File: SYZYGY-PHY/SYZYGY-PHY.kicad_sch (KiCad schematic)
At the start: 49 parts, among them J1 ARJM11C7-502-KB-EW2, J2 Conn_01x11, J3 Conn_01x02, J4 QTH-020-01-X-D-DP-A, U1 GPY111, U2 TXV0106BQBR, U3 TXV0106BQBR, Y1 Crystal_GND24

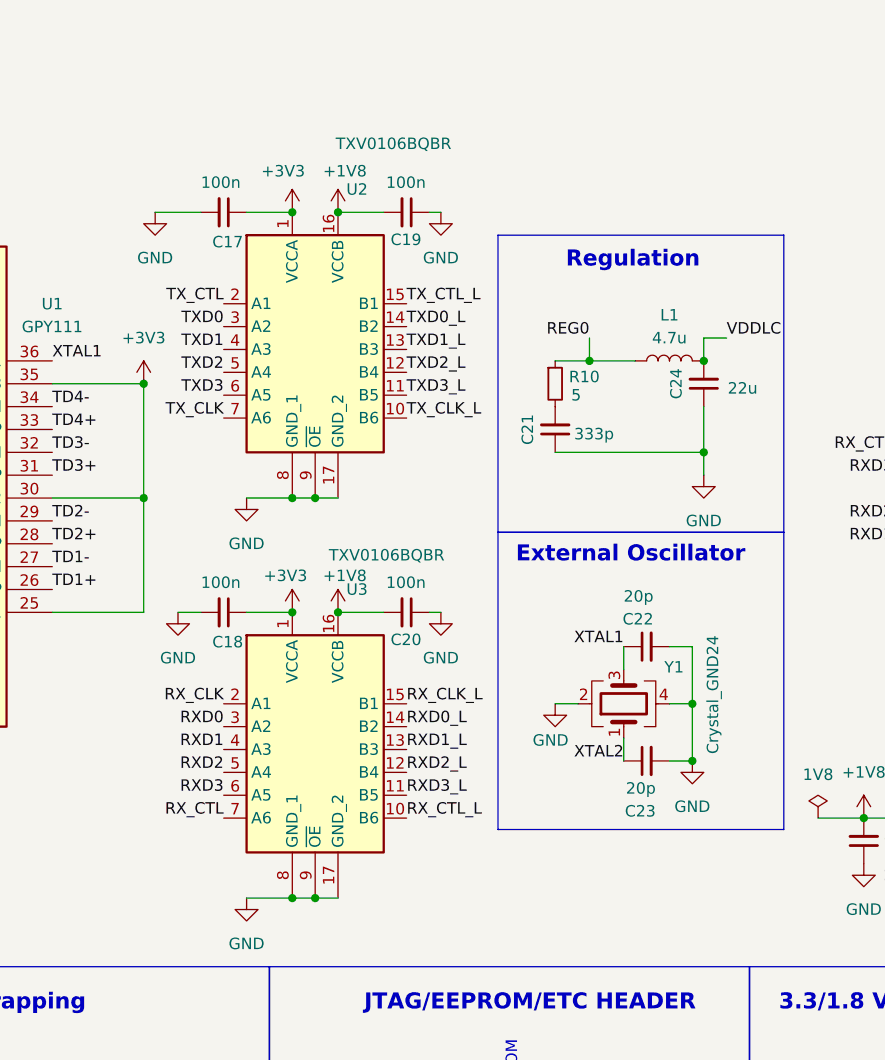
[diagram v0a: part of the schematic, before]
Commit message: busted: backwards level shifter
This snapshot updates the pin assignments such that our TX level shifter
fails the ERC, and then fixes that by flipping it in the schematic.

It also pulls all the updated details from the schematic into the
layout, which does not pass the DRC.
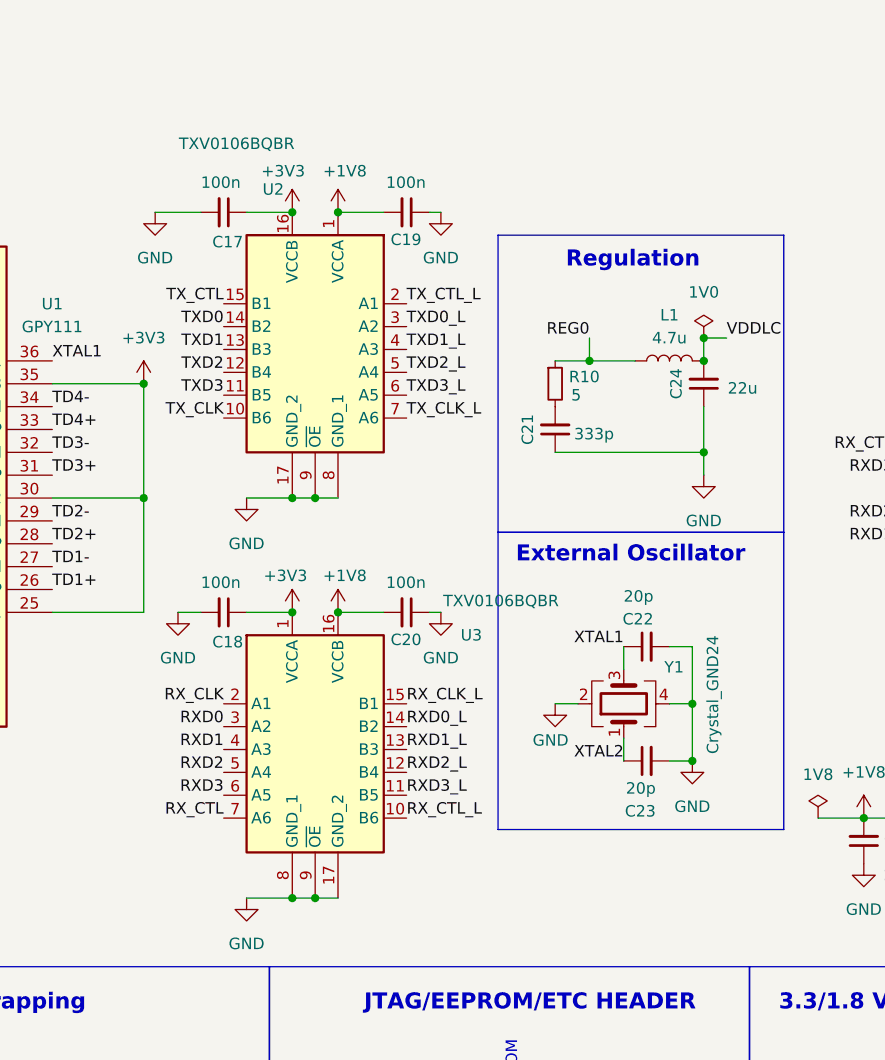
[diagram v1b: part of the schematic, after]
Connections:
- net +1V8: now also U2.1 (VCCA); no longer U2.16 (VCCB)
- net +3V3: now also U2.16 (VCCB); no longer U2.1 (VCCA)
- net TXD0: now also U2.14 (B2); no longer U2.3 (A2)
- net TXD0_L: now also U2.3 (A2); no longer U2.14 (B2)
- net TXD1: now also U2.13 (B3); no longer U2.4 (A3)
- net TXD1_L: now also U2.4 (A3); no longer U2.13 (B3)
- net TXD2: now also U2.12 (B4); no longer U2.5 (A4)
- net TXD2_L: now also U2.5 (A4); no longer U2.12 (B4)
- net TXD3: now also U2.11 (B5); no longer U2.6 (A5)
- net TXD3_L: now also U2.6 (A5); no longer U2.11 (B5)
- net TX_CLK: now also U2.10 (B6); no longer U2.7 (A6)
- net TX_CLK_L: now also U2.7 (A6); no longer U2.10 (B6)
- net TX_CTL: now also U2.15 (B1); no longer U2.2 (A1)
- net TX_CTL_L: now also U2.2 (A1); no longer U2.15 (B1)
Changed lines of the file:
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@@
 	)
 	(junction
-		(at 173.99 111.76)
+		(at 171.45 67.31)
 		(diameter 0)
 		(color 0 0 0 0)
@@
 	)
 	(junction
-		(at 171.45 67.31)
-		(diameter 0)
-		(color 0 0 0 0)
-	)
-	(junction
-		(at 176.53 80.01)
+		(at 140.97 137.16)
 		(diameter 0)
 		(color 0 0 0 0)
 	)
 	(junction
-		(at 140.97 137.16)
+		(at 80.01 31.75)
 		(diameter 0)
 		(color 0 0 0 0)
 	)
 	(junction
-		(at 80.01 31.75)
+		(at 73.66 31.75)
 		(diameter 0)
 		(color 0 0 0 0)
 	)
 	(junction
-		(at 73.66 31.75)
+		(at 173.99 111.76)
 		(diameter 0)
 		(color 0 0 0 0)
@@
 	)
 	(junction
-		(at 173.99 67.31)
+		(at 62.23 87.63)
 		(diameter 0)
 		(color 0 0 0 0)
 	)
 	(junction
-		(at 62.23 87.63)
+		(at 217.17 52.07)
 		(diameter 0)
 		(color 0 0 0 0)
 	)
 	(junction
-		(at 217.17 52.07)
+		(at 176.53 80.01)
 		(diameter 0)
 		(color 0 0 0 0)
@@
 	)
 	(junction
+		(at 171.45 35.56)
+		(diameter 0)
+		(color 0 0 0 0)
+	)
+	(junction
 		(at 60.96 26.67)
 		(diameter 0)
@@
 	)
 	(junction
-		(at 171.45 35.56)
-		(diameter 0)
-		(color 0 0 0 0)
-	)
-	(junction
 		(at 41.91 26.67)
 		(diameter 0)
@@
 	)
 	(junction
-		(at 176.53 35.56)
+		(at 217.17 49.53)
 		(diameter 0)
 		(color 0 0 0 0)
@@
 	)
 	(junction
+		(at 173.99 67.31)
+		(diameter 0)
+		(color 0 0 0 0)
+	)
+	(junction
 		(at 171.45 80.01)
 		(diameter 0)
@@
 	)
 	(junction
+		(at 176.53 35.56)
+		(diameter 0)
+		(color 0 0 0 0)
+	)
+	(junction
 		(at 118.11 154.94)
 		(diameter 0)
@@
 	(wire
 		(pts
-			(xy 171.45 111.76) (xy 173.99 111.76)
-		)
-		(stroke
-			(width 0)
-			(type default)
-		)
-	)
-	(wire
-		(pts
 			(xy 274.32 97.79) (xy 274.32 102.87)
 		)
@@
 	(wire
 		(pts
-			(xy 173.99 111.76) (xy 176.53 111.76)
-		)
-		(stroke
-			(width 0)
-			(type default)
-		)
-	)
-	(wire
-		(pts
 			(xy 156.21 35.56) (xy 161.29 35.56)
 		)
@@
 	(wire
 		(pts
+			(xy 173.99 111.76) (xy 176.53 111.76)
+		)
+		(stroke
+			(width 0)
+			(type default)
+		)
+	)
+	(wire
+		(pts
 			(xy 166.37 80.01) (xy 171.45 80.01)
 		)
@@
 	(wire
 		(pts
-			(xy 171.45 67.31) (xy 173.99 67.31)
+			(xy 173.99 67.31) (xy 176.53 67.31)
 		)
 		(stroke
@@
 	(wire
 		(pts
+			(xy 171.45 67.31) (xy 173.99 67.31)
+		)
+		(stroke
+			(width 0)
+			(type default)
+		)
+	)
+	(wire
+		(pts
 			(xy 114.3 97.79) (xy 114.3 113.03)
 		)
@@
 	(wire
 		(pts
-			(xy 173.99 67.31) (xy 176.53 67.31)
+			(xy 71.12 120.65) (xy 71.12 123.19)
 		)
 		(stroke
@@
 	(wire
 		(pts
-			(xy 71.12 120.65) (xy 71.12 123.19)
+			(xy 116.84 34.29) (xy 116.84 26.67)
 		)
 		(stroke
@@
 	(wire
 		(pts
-			(xy 116.84 34.29) (xy 116.84 26.67)
+			(xy 118.11 154.94) (xy 118.11 158.75)
 		)
 		(stroke
@@
 	(wire
 		(pts
-			(xy 118.11 154.94) (xy 118.11 158.75)
+			(xy 171.45 111.76) (xy 173.99 111.76)
 		)
 		(stroke
@@
 	(symbol
 		(lib_id "TXV0106BQBR:TXV0106BQBR")
-		(at 161.29 90.17 0)
+		(at 173.99 95.25 0)
 		(unit 1)
 		(exclude_from_sim no)
@@
 		(dnp no)
 		(property "Reference" "U3"
-			(at 177.4541 77.47 0)
+			(at 190.1541 82.55 0)
 			(effects
 				(font
@@
 		)
 		(property "Value" "TXV0106BQBR"
-			(at 175.514 73.66 0)
+			(at 188.214 78.74 0)
 			(effects
 				(font
@@
 		)
 		(property "Footprint" "local:TXV0106BQBR"
-			(at 182.88 174.93 0)
+			(at 195.58 180.01 0)
 			(effects
 				(font
@@
 		)
 		(property "Datasheet" "https://www.ti.com/lit/ds/symlink/txv0106.pdf?ts=1710334541958&ref_url=https%253A%252F%252Fwww.ti.com%252Fproduct%252FTXV0106%253FkeyMatch%253DTXV"
-			(at 182.88 274.93 0)
+			(at 195.58 280.01 0)
 			(effects
 				(font
@@
 		)
 		(property "Description" "Voltage Level Translator Unidirectional 1 Circuit 6 Channel 500Mbps 16-WQFN (2.5x3.5)"
-			(at 161.29 90.17 0)
+			(at 173.99 95.25 0)
 			(effects
 				(font
@@
 		)
 		(property "Height" "0.8"
-			(at 182.88 474.93 0)
+			(at 195.58 480.01 0)
 			(effects
 				(font
@@
 		)
 		(property "Mouser Part Number" "595-TXV0106BQBR"
-			(at 182.88 574.93 0)
+			(at 195.58 580.01 0)
 			(effects
 				(font
@@
 		)
 		(property "Mouser Price/Stock" "https://www.mouser.co.uk/ProductDetail/Texas-Instruments/TXV0106BQBR?qs=mELouGlnn3c1YOKCKwursg%3D%3D"
-			(at 182.88 674.93 0)
+			(at 195.58 680.01 0)
 			(effects
 				(font
@@
 		)
 		(property "Manufacturer_Name" "Texas Instruments"
-			(at 182.88 774.93 0)
+			(at 195.58 780.01 0)
 			(effects
 				(font
@@
 		)
 		(property "Manufacturer_Part_Number" "TXV0106BQBR"
-			(at 182.88 874.93 0)
+			(at 195.58 880.01 0)
 			(effects
 				(font
@@
 	(symbol
 		(lib_id "TXV0106BQBR:TXV0106BQBR")
-		(at 161.29 45.72 0)
+		(at 173.99 50.8 0)
+		(mirror y)
 		(unit 1)
 		(exclude_from_sim no)
@@
 		(dnp no)
 		(property "Reference" "U2"
-			(at 177.4541 33.02 0)
+			(at 170.5259 33.02 0)
 			(effects
 				(font
@@
 		)
 		(property "Value" "TXV0106BQBR"
-			(at 176.276 27.94 0)
+			(at 171.704 27.94 0)
 			(effects
 				(font
@@
 		)
 		(property "Footprint" "local:TXV0106BQBR"
-			(at 182.88 130.48 0)
+			(at 152.4 135.56 0)
 			(effects
 				(font
@@
 		)
 		(property "Datasheet" "https://www.ti.com/lit/ds/symlink/txv0106.pdf?ts=1710334541958&ref_url=https%253A%252F%252Fwww.ti.com%252Fproduct%252FTXV0106%253FkeyMatch%253DTXV"
-			(at 182.88 230.48 0)
+			(at 152.4 235.56 0)
 			(effects
 				(font
@@
 		)
 		(property "Description" "Voltage Level Translator Unidirectional 1 Circuit 6 Channel 500Mbps 16-WQFN (2.5x3.5)"
-			(at 161.29 45.72 0)
+			(at 174.244 49.53 0)
 			(effects
 				(font
@@
 		)
 		(property "Height" "0.8"
-			(at 182.88 430.48 0)
+			(at 152.4 435.56 0)
 			(effects
 				(font
@@
 		)
 		(property "Mouser Part Number" "595-TXV0106BQBR"
-			(at 182.88 530.48 0)
+			(at 152.4 535.56 0)
 			(effects
 				(font
@@
 		)
 		(property "Mouser Price/Stock" "https://www.mouser.co.uk/ProductDetail/Texas-Instruments/TXV0106BQBR?qs=mELouGlnn3c1YOKCKwursg%3D%3D"
-			(at 182.88 630.48 0)
+			(at 152.4 635.56 0)
 			(effects
 				(font
@@
 		)
 		(property "Manufacturer_Name" "Texas Instruments"
-			(at 182.88 730.48 0)
+			(at 152.4 735.56 0)
 			(effects
 				(font
@@
 		)
 		(property "Manufacturer_Part_Number" "TXV0106BQBR"
-			(at 182.88 830.48 0)
+			(at 152.4 835.56 0)
 			(effects
 				(font
@@
 					(unit 1)
 				)
+			)
+		)
+	)
+	(symbol
+		(lib_id "power:PWR_FLAG")
+		(at 217.17 49.53 0)
+		(unit 1)
+		(exclude_from_sim no)
+		(in_bom yes)
+		(on_board yes)
+		(dnp no)
+		(fields_autoplaced yes)
+		(property "Reference" "#FLG06"
+			(at 217.17 47.625 0)
+			(effects
+				(font
+					(size 1.27 1.27)
+				)
+				(hide yes)
+			)
+		)
+		(property "Value" "1V0"
+			(at 217.17 44.45 0)
+			(effects
+				(font
+					(size 1.27 1.27)
+				)
+			)
+		)
+		(property "Footprint" ""
+			(at 217.17 49.53 0)
+			(effects
+				(font
+					(size 1.27 1.27)
+				)
+				(hide yes)
+			)
+		)
+		(property "Datasheet" "~"
+			(at 217.17 49.53 0)
+			(effects
+				(font
+					(size 1.27 1.27)
+				)
+				(hide yes)
+			)
+		)
+		(property "Description" "Special symbol for telling ERC where power comes from"
+			(at 217.17 49.53 0)
+			(effects
+				(font
+					(size 1.27 1.27)
+				)
+				(hide yes)
+			)
+		)
+		(pin "1"
+		)
+		(instances
+			(project ""
+				(path "/cd7d6255-0cd2-43fc-ba6e-5ac7b6205d5d"
+					(reference "#FLG06")
+					(unit 1)
+				)

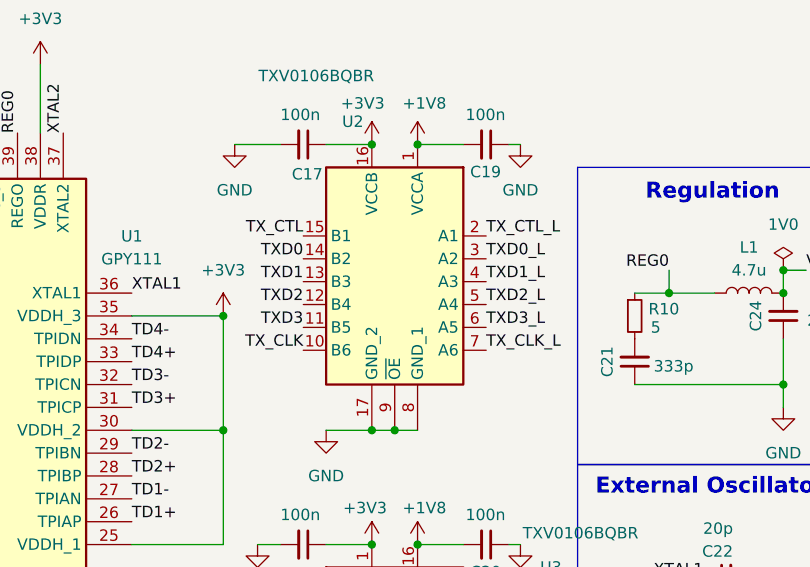
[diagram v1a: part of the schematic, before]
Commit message: flipping the level shifter adding some labels
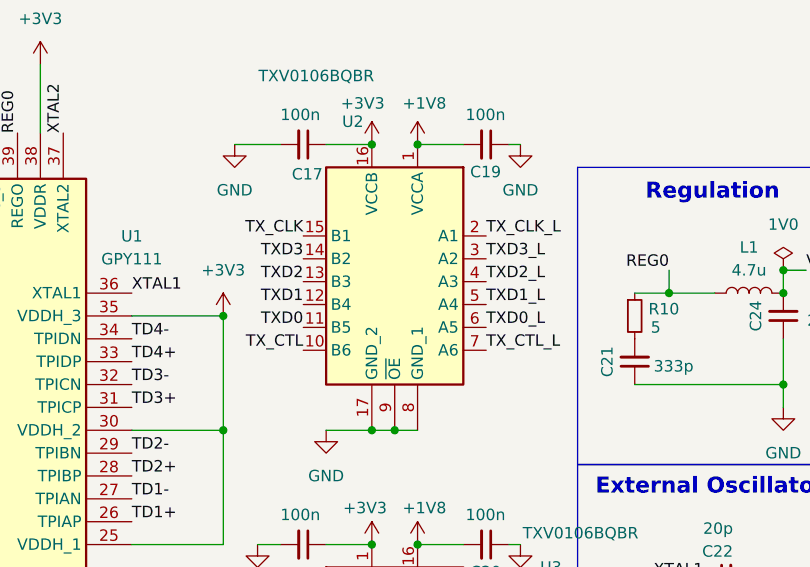
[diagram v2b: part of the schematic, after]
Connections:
- net TXD0: now also U2.11 (B5); no longer U2.14 (B2)
- net TXD0_L: now also U2.6 (A5); no longer U2.3 (A2)
- net TXD1: now also U2.12 (B4); no longer U2.13 (B3)
- net TXD1_L: now also U2.5 (A4); no longer U2.4 (A3)
- net TXD2: now also U2.13 (B3); no longer U2.12 (B4)
- net TXD2_L: now also U2.4 (A3); no longer U2.5 (A4)
- net TXD3: now also U2.14 (B2); no longer U2.11 (B5)
- net TXD3_L: now also U2.3 (A2); no longer U2.6 (A5)
- net TX_CLK: now also U2.15 (B1); no longer U2.10 (B6)
- net TX_CLK_L: now also U2.2 (A1); no longer U2.7 (A6)
- net TX_CTL: now also U2.10 (B6); no longer U2.15 (B1)
- net TX_CTL_L: now also U2.7 (A6); no longer U2.2 (A1)
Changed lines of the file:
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@@
 	)
 	(label "TX_CLK_L"
-		(at 184.15 58.42 0)
+		(at 184.15 45.72 0)
 		(fields_autoplaced yes)
 		(effects
@@
 	)
 	(label "TX_CLK"
-		(at 163.83 58.42 180)
+		(at 163.83 45.72 180)
 		(fields_autoplaced yes)
 		(effects
@@
 	)
 	(label "TXD2_L"
-		(at 184.15 53.34 0)
+		(at 184.15 50.8 0)
 		(fields_autoplaced yes)
 		(effects
@@
 	)
 	(label "TX_CTL_L"
-		(at 184.15 45.72 0)
+		(at 184.15 58.42 0)
 		(fields_autoplaced yes)
 		(effects
@@
 	)
 	(label "TXD1_L"
-		(at 184.15 50.8 0)
+		(at 184.15 53.34 0)
 		(fields_autoplaced yes)
 		(effects
@@
 	)
 	(label "TXD1"
-		(at 163.83 50.8 180)
+		(at 163.83 53.34 180)
 		(fields_autoplaced yes)
 		(effects
@@
 	)
 	(label "TX_CTL"
-		(at 163.83 45.72 180)
+		(at 163.83 58.42 180)
 		(fields_autoplaced yes)
 		(effects
@@
 	)
 	(label "TXD0_L"
-		(at 184.15 48.26 0)
+		(at 184.15 55.88 0)
 		(fields_autoplaced yes)
 		(effects
@@
 	)
 	(label "TXD0"
-		(at 163.83 48.26 180)
+		(at 163.83 55.88 180)
 		(fields_autoplaced yes)
 		(effects
@@
 	)
 	(label "TXD3"
-		(at 163.83 55.88 180)
+		(at 163.83 48.26 180)
 		(fields_autoplaced yes)
 		(effects
@@
 	)
 	(label "TXD2"
-		(at 163.83 53.34 180)
+		(at 163.83 50.8 180)
 		(fields_autoplaced yes)
 		(effects
@@
 	)
 	(label "TXD3_L"
-		(at 184.15 55.88 0)
-		(fields_autoplaced yes)
-		(effects
+		(at 184.15 48.26 0)
+		(fields_autoplaced yes)
+		(effects
